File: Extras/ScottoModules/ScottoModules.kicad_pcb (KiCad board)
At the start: 4 copper layers, 57.2 x 57.1 mm, 27 parts, among them J1 USB_C, SW1 SW_Push, U1 STM32F072CBT6, U3 XC6206, U4 USBLC6-2SC6

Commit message: Finalize modules
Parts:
- moved R1 24.9 mm to (428.0, 50.9)
- moved SW1 20.4 mm to (430.3, 56.1), turned to 90 degrees
- moved C6 12.5 mm to (436.5, 71.3), turned to 180 degrees
- moved C8 3.16 mm to (435.8, 51.3), turned to 180 degrees
- moved C9 2.94 mm to (434.2, 56.2), turned to 0 degrees
- moved C1 2.67 mm to (434.4, 80.0), turned to 180 degrees
- moved C7 1.91 mm to (430.6, 81.4), turned to -90 degrees
- moved U3 1.06 mm to (435.0, 53.8)
- moved C2 0.88 mm to (429.6, 81.4), turned to 90 degrees
- moved C5 0.64 mm to (435.0, 78.9), turned to 180 degrees
- moved C3 0.64 mm to (426.0, 71.1), turned to -90 degrees
- moved R3 0.62 mm to (432.4, 42.7), turned to 0 degrees
- moved R2 0.62 mm to (428.1, 42.7), turned to 180 degrees
- moved F1 0.50 mm to (432.8, 45.5)
- moved C4 0.23 mm to (434.5, 71.1), turned to 90 degrees
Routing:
- net D+: track 15.9 -> 23.6 mm
- net D-: track 16.0 -> 23.7 mm
- net BOOT0: track 15.0 -> 8.55 mm
- net +3.3V: track 40.8 -> 46.8 mm, vias 5 -> 0
- net GND: track 22.0 -> 23.5 mm, vias 18 -> 16
- net +5V: track 16.7 -> 15.4 mm, vias 3 -> 2
- net Net-(U1-NRST): track 2.94 -> 1.70 mm
- removed copper zone on In1.Cu, net GND
- removed copper zone on In2.Cu, net GND
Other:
- copper layers 4 -> 2

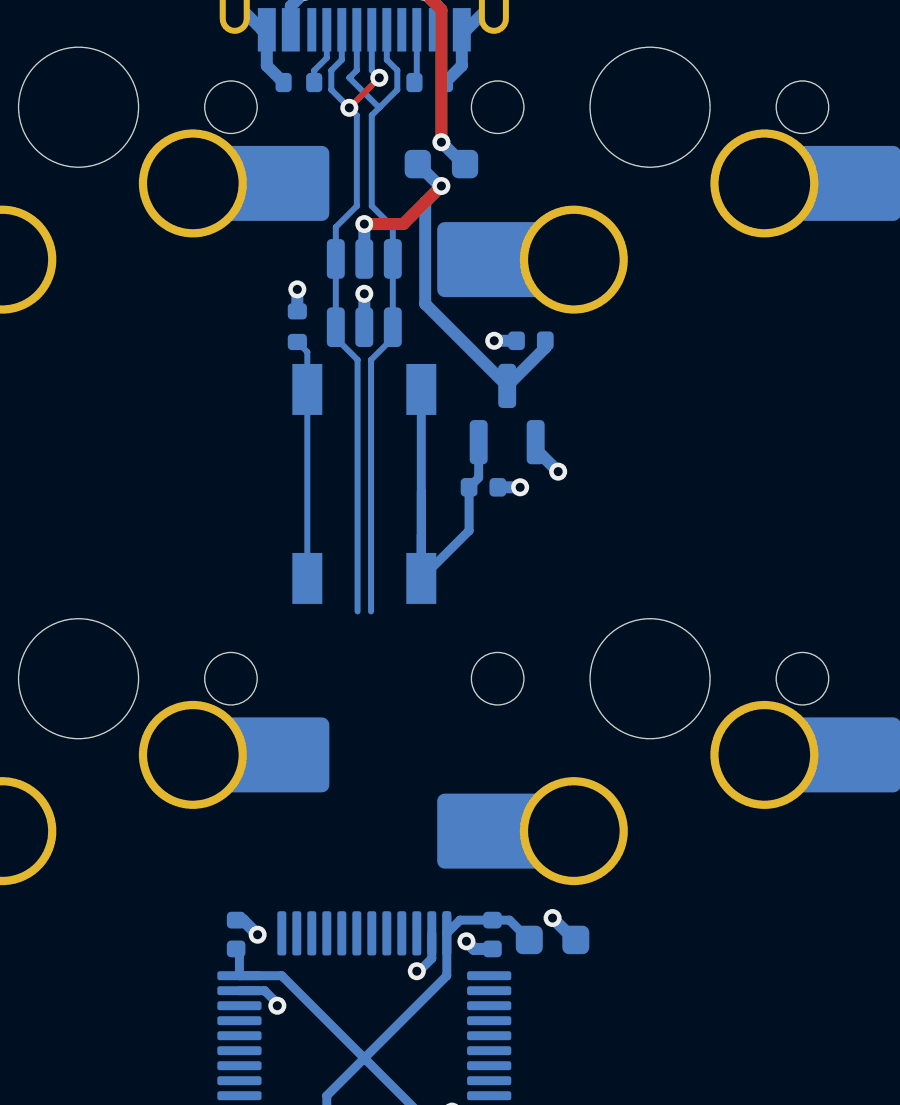
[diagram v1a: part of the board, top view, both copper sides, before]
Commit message: Update Cap placement for regulator
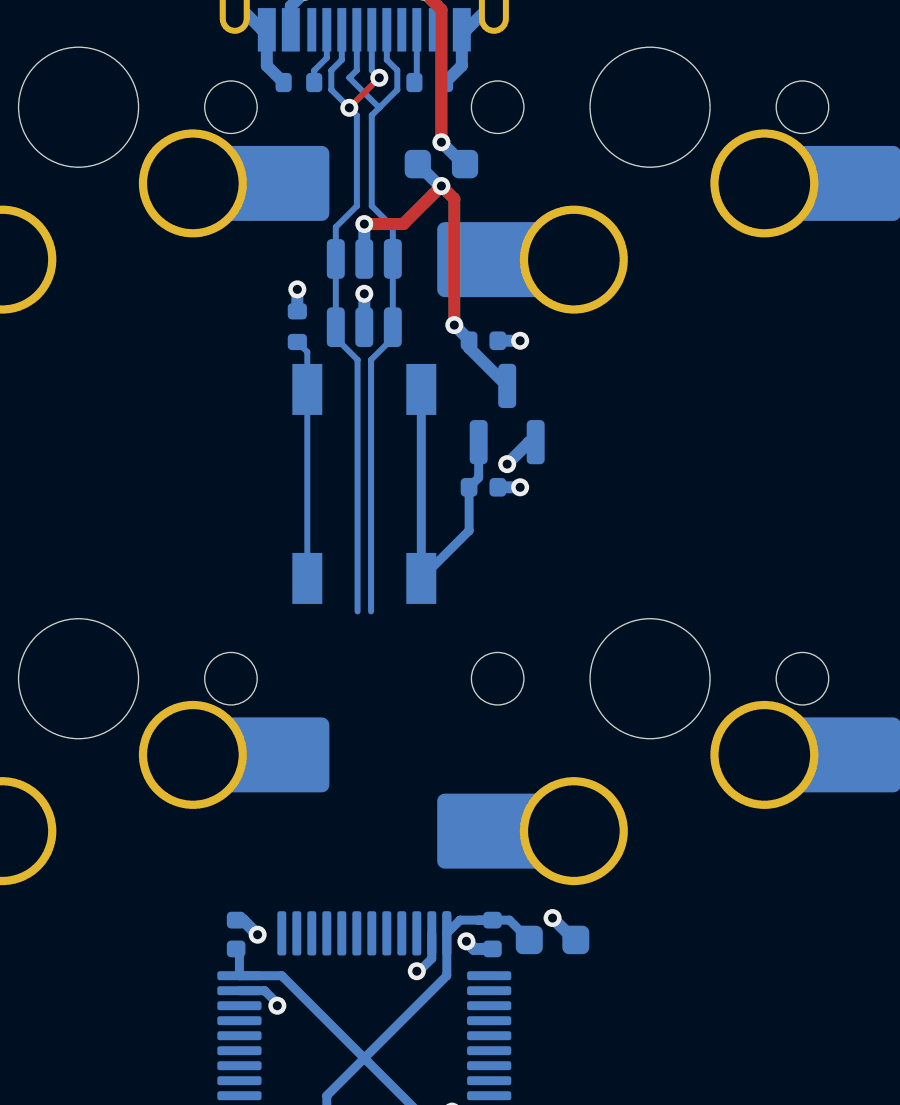
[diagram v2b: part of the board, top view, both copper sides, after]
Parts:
- moved C8 1.58 mm to (434.2, 51.3), turned to 0 degrees
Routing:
- net +3.3V: track 46.8 -> 43.2 mm
- net +5V: track 15.4 -> 13.7 mm, vias 2 -> 3

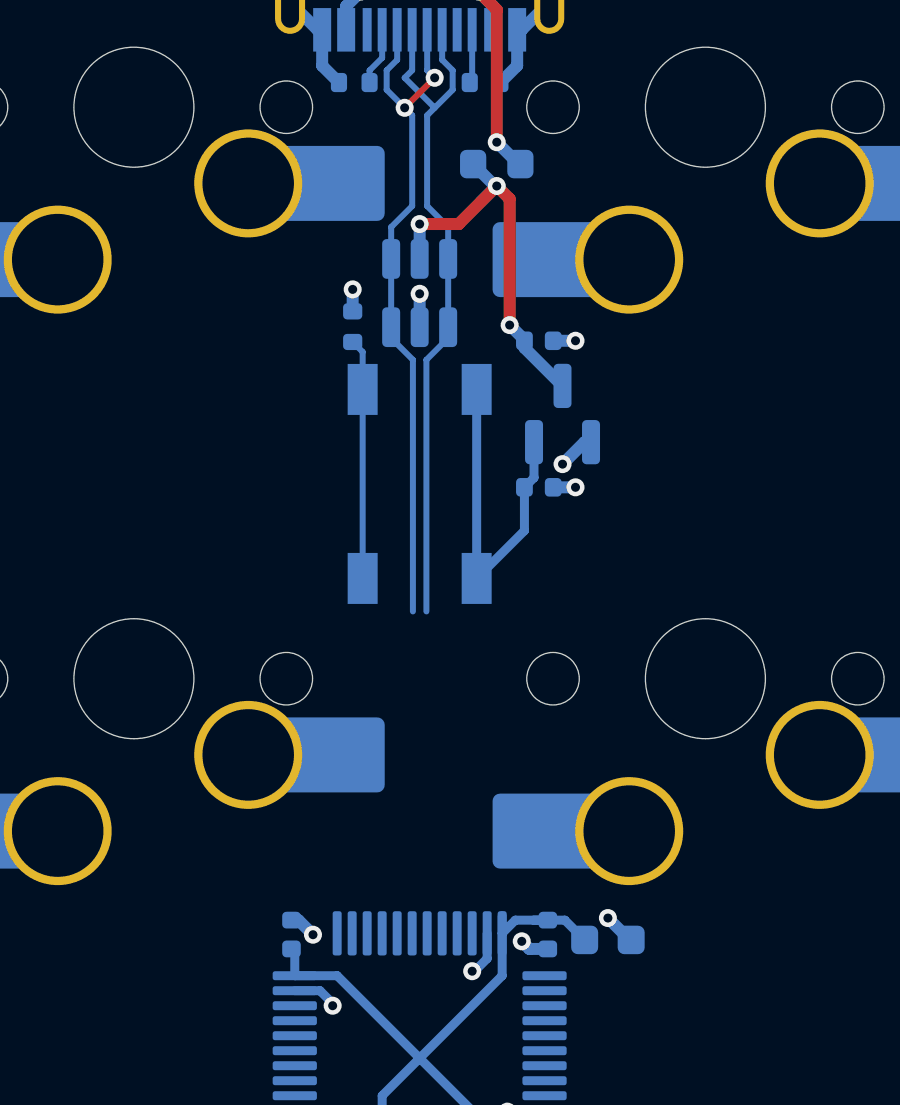
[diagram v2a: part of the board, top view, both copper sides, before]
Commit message: Fix unconnected tracks
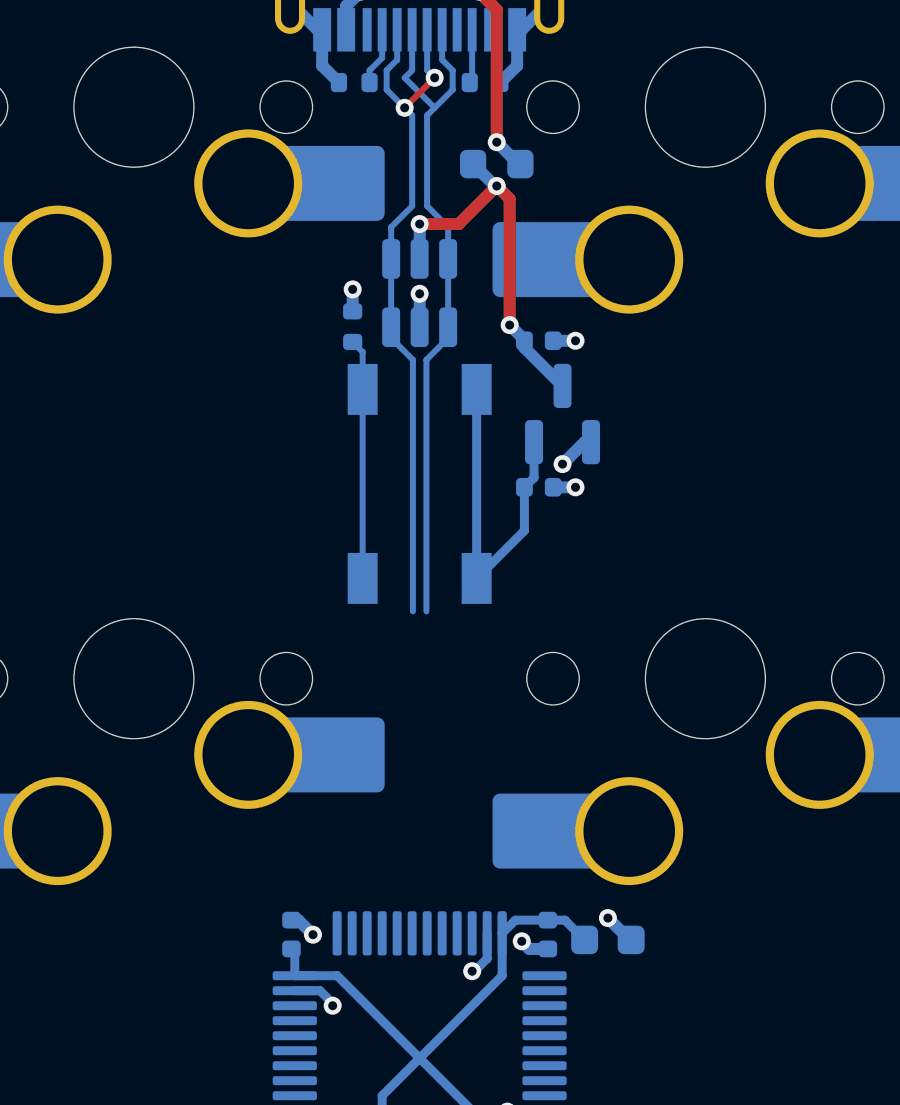
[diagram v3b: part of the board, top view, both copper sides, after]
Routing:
- net +5V: track 13.7 -> 12.9 mm
